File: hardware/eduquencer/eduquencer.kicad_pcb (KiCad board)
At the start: 2 copper layers, 71.1 x 128.5 mm, 166 parts, among them IC1 MCP23018-E_SO, IC2 MCP23018-E_SO, IC3 SN74AHCT244NSR, IC4 ADP150AUJZ-3.3-R7, IC5 DAC80501MDGST, IC6 OPA172IDR, J1 Debug, J10 Out 6, J11 Out 4, J12 Out 5, J13 Eurorack PWR, J14 Out A, J2 Clock In, J3 Reset In, J4 CV In A, J5 CV In B, J6 Out 1, J7 Out 2, J8 Out 7, J9 Out 3, Q1 MMBT3904, Q2 MMBT3904, SW1 COM-12992, SW10 COM-12992, SW11 COM-12992, SW12 COM-12992, SW13 COM-12992, SW14 COM-12992, SW15 COM-12992, SW16 COM-12992, SW2 COM-12992, SW3 COM-12992, SW4 COM-12992, SW5 COM-12992, SW6 COM-12992, SW7 COM-12992, SW8 COM-12992, SW9 COM-12992, U1 Pico, U2 TL074, U3 MCP6002-xMS, U5 LM1117-5.0, U6 LM4040DBZ-10, U7 LM4040DBZ-5

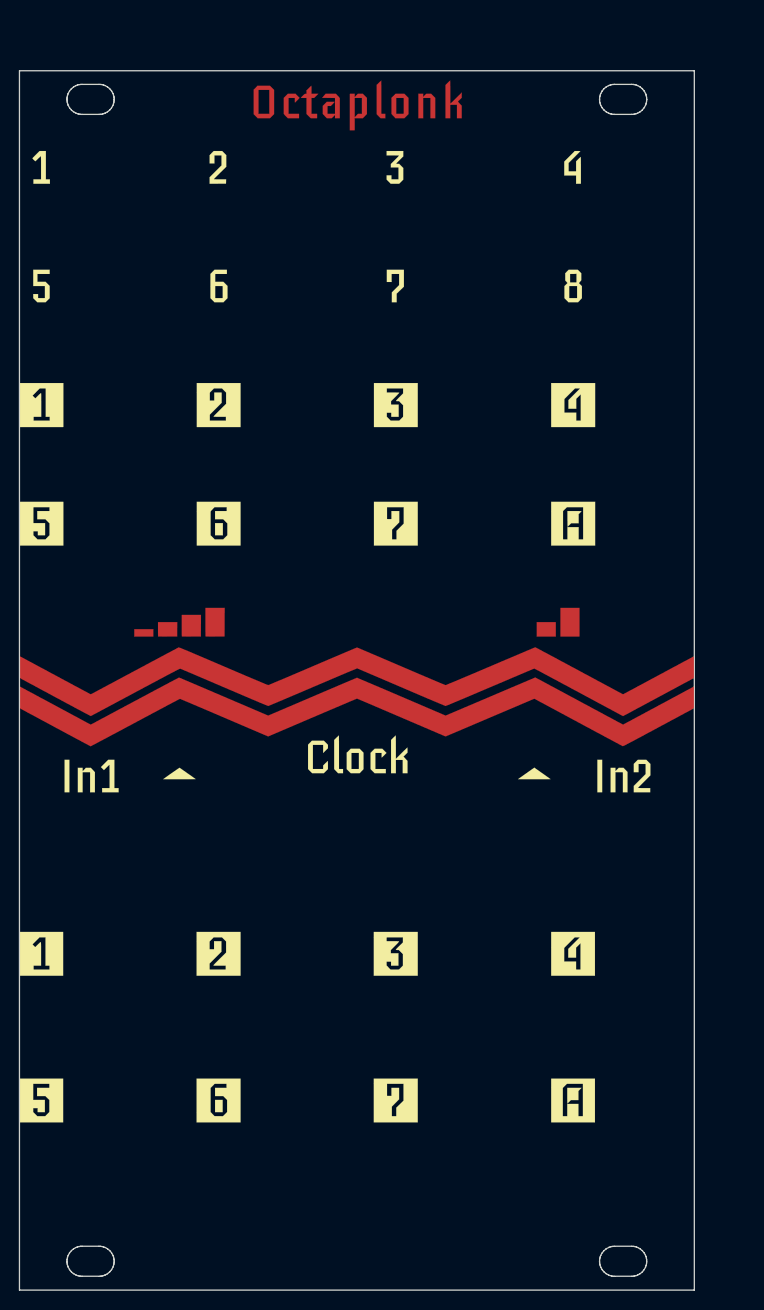
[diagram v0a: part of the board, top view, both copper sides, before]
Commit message: Update board footprint on board
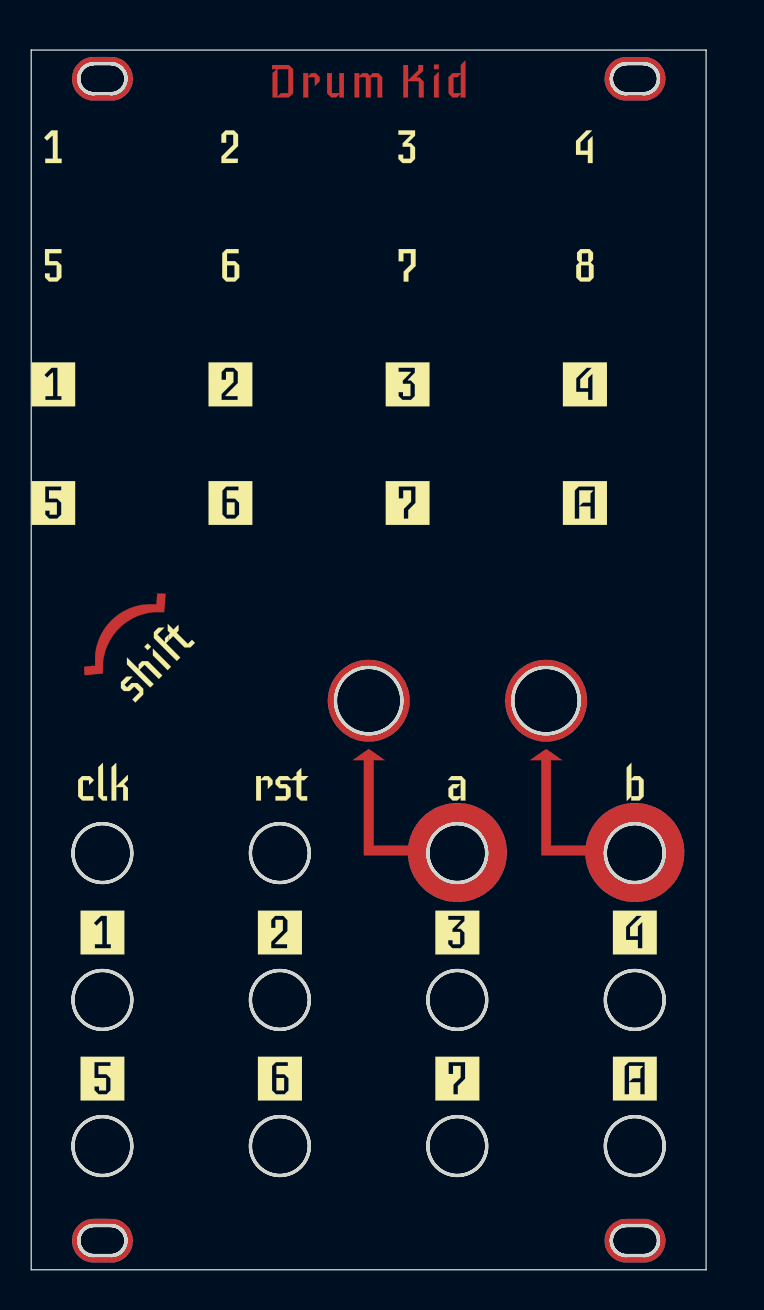
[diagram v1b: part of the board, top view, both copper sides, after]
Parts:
- moved Ref** 2.51 mm to (24.1, 91.8)
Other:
- outline, holes or cut-outs redrawn
